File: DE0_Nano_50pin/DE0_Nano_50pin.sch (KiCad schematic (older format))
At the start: 99 parts, among them M1 4-40, M2 4-40, M3 4-40, M4 4-40, P2 CONN_25X2, P3 CONN_25X2, P4 CONN_25X2

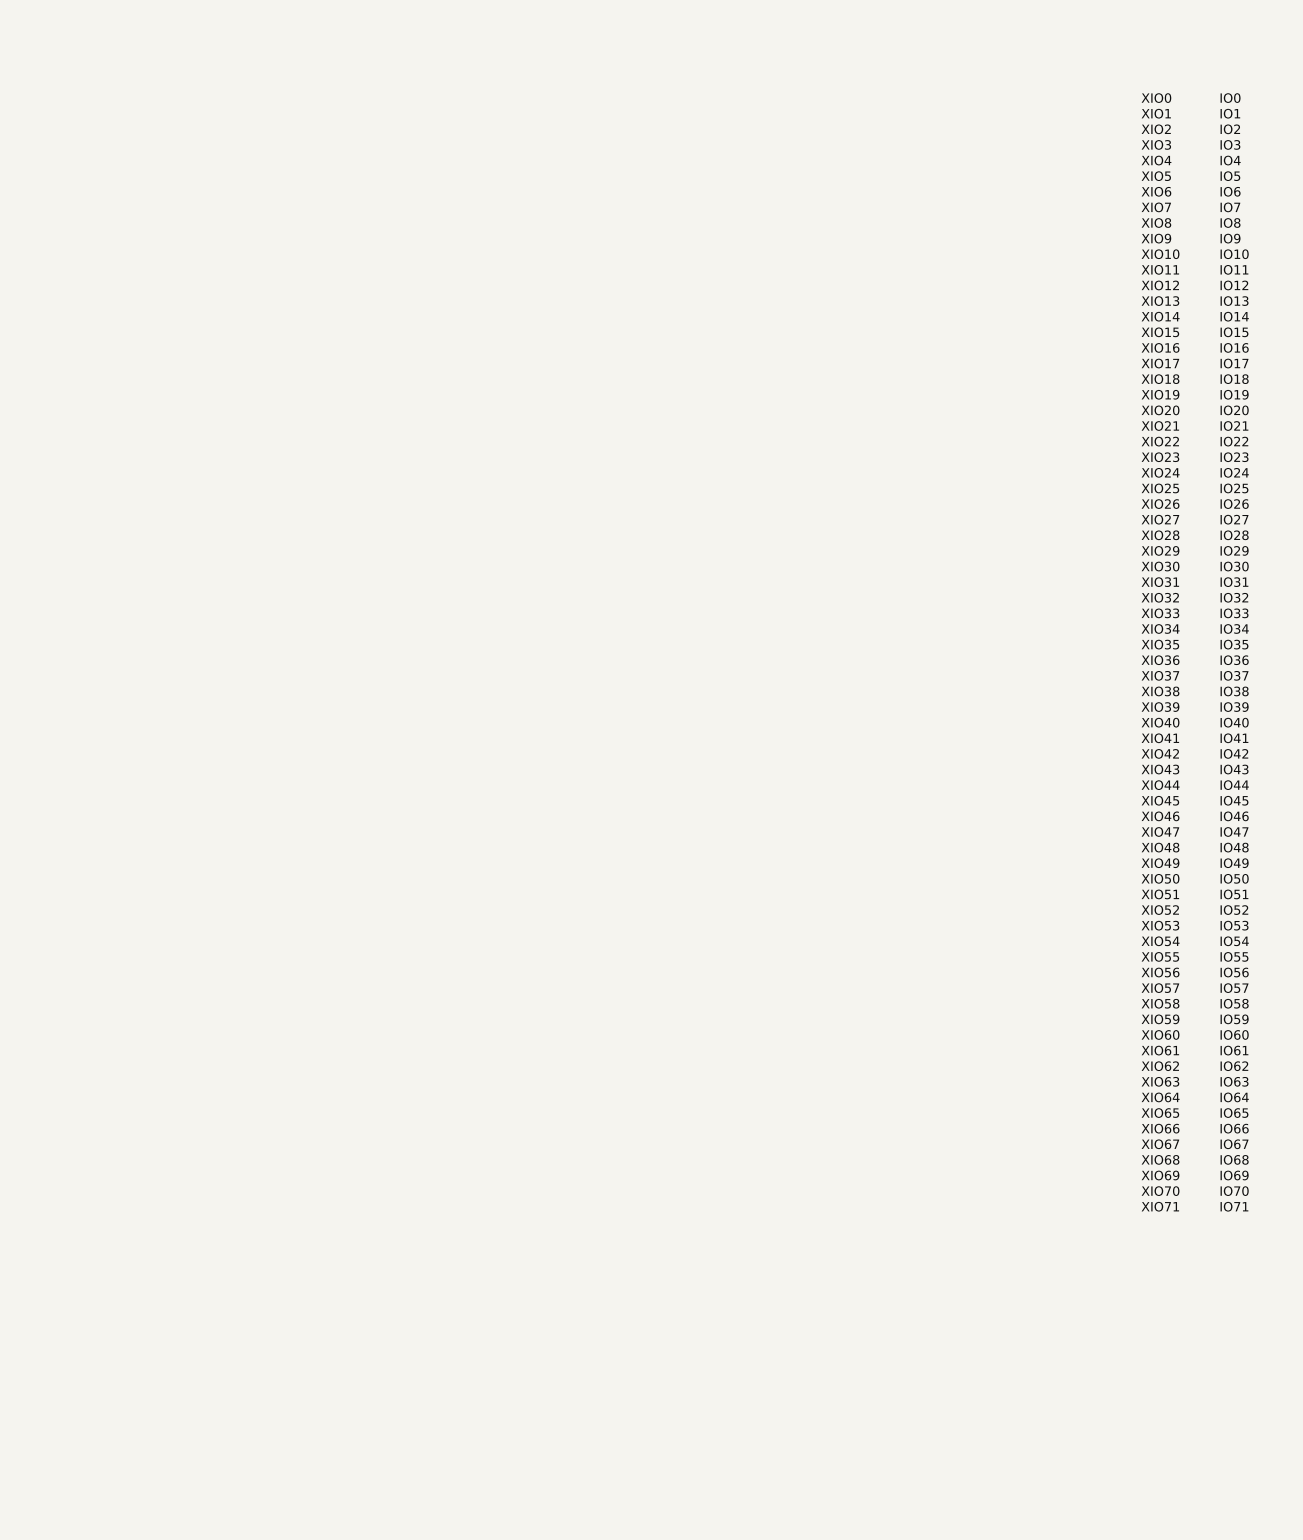
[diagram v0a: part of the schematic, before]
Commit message: Update level translators
Switch to 74CBTD16211 level transators in SOP package

Signed-off-by: Charles Steinkuehler <charles@steinkuehler.net>
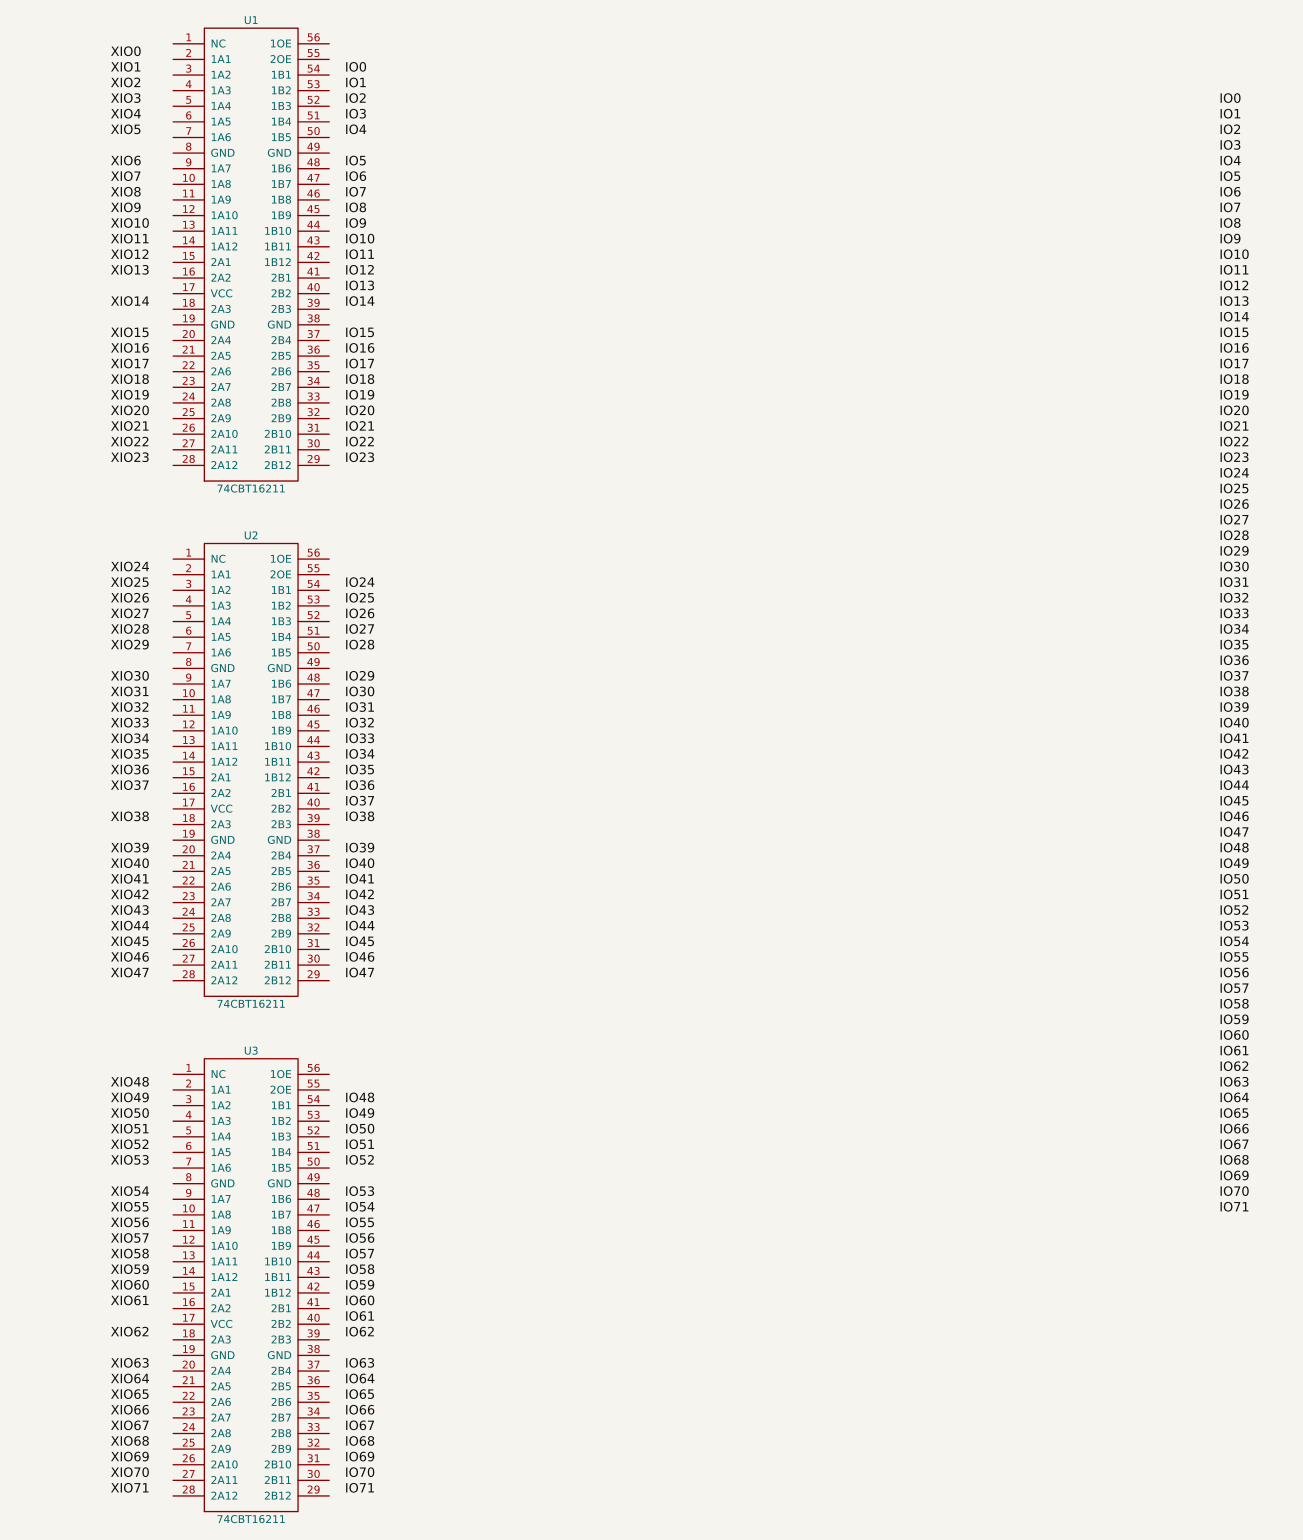
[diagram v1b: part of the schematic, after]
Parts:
- added U1, U2, U3: 74CBT16211, SOP63P1035X279-56N, symbol 74CBT16211

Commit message: DE0_Nano_50pin/DE0_Nano_50pin.sch: connect level pins to 50pin
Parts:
- S1, S2, S3: symbol SHUNT -> Shunt
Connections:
- wire segments 362 -> 506
